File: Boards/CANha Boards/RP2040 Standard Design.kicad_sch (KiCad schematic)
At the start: 37 parts, among them J17 USB_C, J7 BM03B-SRSS-TBLFSN, SW2 SW_Push, SW3 SW_Push, U6 ESD7L5.0DT5G, U7 ST1L05APU33R

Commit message: Algumas correções ERC e ajustes no Design dos DCDC
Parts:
- removed FlashM1: W25Q128JVSIQ_TR, SOIC_208MIL_WIN, symbol W25Q128JVSIQ TR:W25Q128JVSIQ_TR
- removed J17: USB_C, Connector_USB:USB_C_Plug_JAE_DX07P024AJ1, symbol Connector:USB_C_Receptacle_USB2.0
- removed J7: BM03B-SRSS-TBLFSN, CONN_BM03B-SRSS-TBLFSN_JST, symbol SWD Con:BM03B-SRSS-TBLFSN
- removed SW2, SW3: SW_Push, Button_Switch_SMD:SW_Push_1P1T-MP_NO_Horizontal_Alps_SKRTLAE010, symbol Switch:SW_Push
- removed U6: ESD7L5.0DT5G, SOT-723_0P85X1P25_ONS, symbol ESD Protection Diode:ESD7L5.0DT5G
- removed U7: ST1L05APU33R, DFN_5APU33R_STM, symbol LDO 5V.3V3:ST1L05APU33R
- removed XTAL1: ASE-12.000MHZ-LC-T, ASE-3.2X2.5_ABR, symbol AS12MHz:ASE-12.000MHZ-LC-T
- added J17: USB_C_Receptacle_USB2.0_14P, symbol Connector:USB_C_Receptacle_USB2.0_14P
- added J7: BM03B-SRSS-TBLFSN, CONN_BM03B-SRSS-TBLFSN_JST, symbol SWD Connector:BM03B-SRSS-TBLFSN
- added S3, S4: TL3305CF160QG, TL3305CF160QG:SW_TL3305CF160QG, symbol TL3305CF160QG:TL3305CF160QG
- added U18: ST1L05APU33R, DFN_5APU33R_STM, symbol LDO 5V 3V3:ST1L05APU33R
- added U6: W25Q128JVSIQ TR, SOIC_208MIL_WIN, symbol 16MB Flash Memory:W25Q128JVSIQ_TR
- added U7: ESD7L5.0DT5G, SOT-723_0P85X1P25_ONS, symbol ESD Diodes:ESD7L5.0DT5G
- added XTAL1: ASE-12.000MHZ-LC-T, ASE-3.2X2.5_ABR, symbol Powered Crystal:ASE-12.000MHZ-LC-T
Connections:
- net +3.3V: now also U18.2 (V0), U6.8 (VCC), XTAL1.4 (VDD)
- net +5V: now also J17.A4 (VBUS), J17.A9 (VBUS), J17.B4 (VBUS), J17.B9 (VBUS), U18.3 (V1)
- net CRYSTAL: now also XTAL1.3 (OUTPUT)
- net GND: now also J17.A1 (GND), J17.A12 (GND), J17.B1 (GND), J17.B12 (GND), J7.2, S3.2, S4.2, U18.6 (GND), U18.7 (GND), U6.4 (GND), U7.3, XTAL1.2 (GND/CASE)
- net MCU QSPI_SCLK: now also U6.6 (CLK)
- net MCU QSPI_SD0: now also U6.5 (DI(IO0))
- net MCU QSPI_SD1: now also U6.2 (DO(IO1))
- net MCU QSPI_SD2: now also U6.3 (/WP(IO2))
- net MCU QSPI_SD3: now also U6.7 (/HOLD_/RESET)
- net MCU QSPI_SS: now also U6.1 (/CS)
- net USB_DM: now also J17.A7 (D-), J17.B7 (D-), U7.1
- net USB_DP: now also J17.A6 (D+), J17.B6 (D+), U7.2
- net ~{RST}: now also S3.4
- net ~{USB_BOOT}: now also S4.4
- net at R37.1: now also XTAL1.1 (TRI-STATE(STBY))
- net at R25.1: now also J7.3
- net at R35.1: now also J7.1
- net at R39.2: now also J17.A5 (CC1)
- net at RC1.2: now also J17.B5 (CC2)
- no-connect marks 4 -> 6

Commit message: pequenas alterações, implementação do sensor de temperatura na placa de comunicações
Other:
- company: (none) -> Porto Space Team
- title: (none) -> RP2040 Standard
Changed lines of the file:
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@@
 	(generator_version "8.0")
 	(paper "A4")
+	(title_block
+		(title "RP2040 Standard")
+		(company "Porto Space Team")
+		(comment 1 "Miguel Amorim")
+	)
 	(junction
 		(at 45.72 70.485)

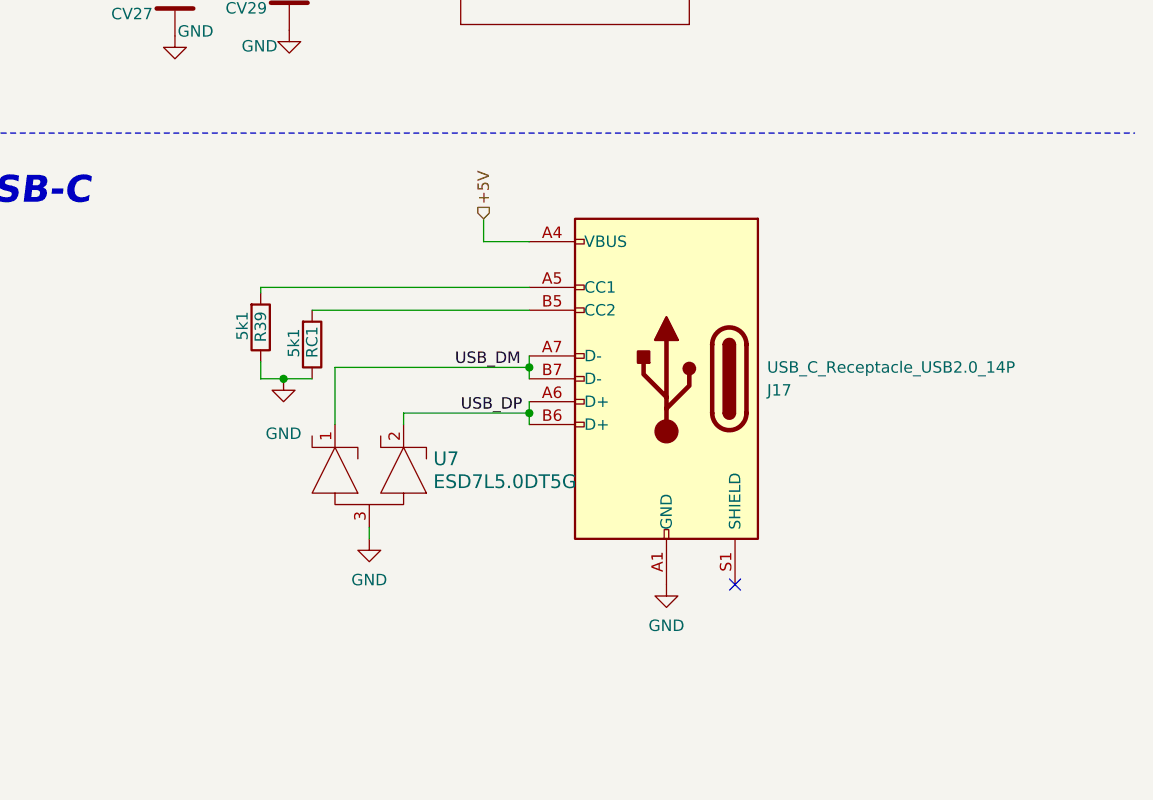
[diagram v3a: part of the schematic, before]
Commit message: USB-C update
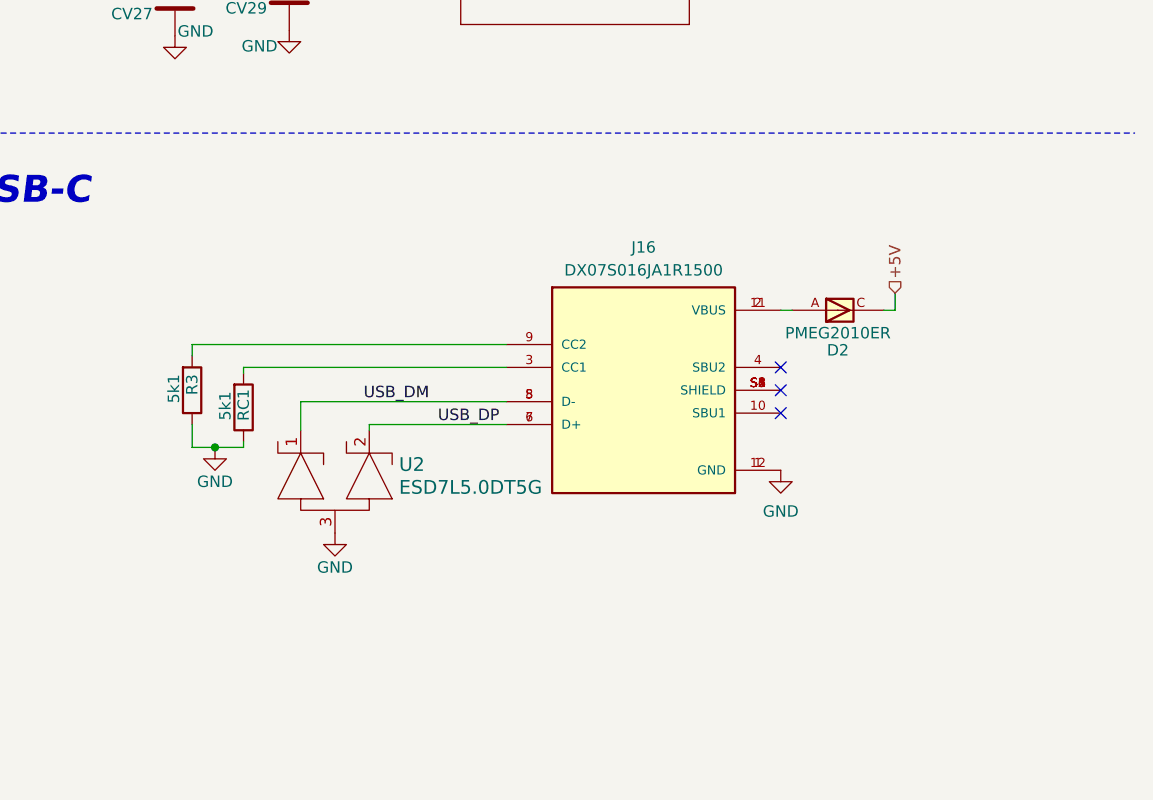
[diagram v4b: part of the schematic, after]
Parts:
- removed J17: USB_C_Receptacle_USB2.0_14P, symbol Connector:USB_C_Receptacle_USB2.0_14P
- removed R39: 5k1, Resistor_SMD:R_0201_0603Metric, symbol Device:R
- removed U7: ESD7L5.0DT5G, SOT-723_0P85X1P25_ONS, symbol ESD Diodes:ESD7L5.0DT5G
- added D2: PMEG2010ER, PMEG2010ER:SODFL3517X110N, symbol Schottky Diode:PMEG2010ER
- added J16: DX07S016JA1R1500, DX07S016JA1R1500:JAE_DX07S016JA1R1500, symbol DX07S016JA1R1500:DX07S016JA1R1500
- added R3: 5k1, Resistor_SMD:R_0201_0603Metric, symbol Device:R
- added U2: ESD7L5.0DT5G, SOT-723_0P85X1P25_ONS, symbol ESD Diodes:ESD7L5.0DT5G
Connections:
- net +5V: now also D2.C
- net GND: now also J16.1 (GND), J16.12 (GND), R3.1, U2.3
- net USB_DM: now also J16.5 (D-), J16.8 (D-), U2.1
- net USB_DP: now also J16.6 (D+), J16.7 (D+), U2.2
- net at RC1.2: now also J16.3 (CC1)
- new net: D2.A, J16.11 (VBUS), J16.2 (VBUS)
- new net: J16.9 (CC2), R3.2
- new net: J16.S1 (SHIELD), J16.S2 (SHIELD), J16.S3 (SHIELD), J16.S4 (SHIELD), J16.S5 (SHIELD), J16.S6 (SHIELD)
- no-connect marks 6 -> 8

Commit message: Atualização CANha
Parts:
- CV13, CV14, CV15, CV16, CV17, CV18, CV19, CV20, CV21, CV22, CV23, CV24, CV25, CV26, CV29, CV30: footprint Capacitor_SMD:C_0201_0603Metric -> CAP_GCM155_MUR:CAP_GCM155_MUR
- CV27, CV28: footprint Capacitor_SMD:C_0201_0603Metric -> GRM15x:GRM15x
- J16: footprint DX07S016JA1R1500:JAE_DX07S016JA1R1500 -> USBC-DX07S016JA1:JAE_DX07S016JA1R1500
- J7: footprint CONN_BM03B-SRSS-TBLFSN_JST -> SWD_Con:CONN_BM03B-SRSS-TBLFSN_JST
- R22, R23, R24, R25, R3, R35, R36, R37, R38: footprint Resistor_SMD:R_0201_0603Metric -> RC0402N_VIS:RC0402N_VIS
- RC1: footprint Resistor_SMD:R_0201_0603Metric -> ERA6AEB101V:ERA6AEB101V
- S3, S4: footprint TL3305CF160QG:SW_TL3305CF160QG -> E-Switch_7mm:SW_TL3305CF160QG
- U18: footprint DFN_5APU33R_STM -> LDO ST1L05A:DFN_5APU33R_STM
- U2: footprint SOT-723_0P85X1P25_ONS -> ESD7L5-Diode:SOT-723_0P85X1P25_ONS
- U6: footprint SOIC_208MIL_WIN -> NOR Flash:SOIC_208MIL_WIN
- XTAL1: footprint ASE-3.2X2.5_ABR -> AS12MHz:ASE-3.2X2.5_ABR
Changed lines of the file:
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@@
 			)
 		)
-		(property "Footprint" "Capacitor_SMD:C_0201_0603Metric"
+		(property "Footprint" "CAP_GCM155_MUR:CAP_GCM155_MUR"
 			(at 129.2352 50.165 0)
 			(effects
@@
 			)
 		)
-		(property "Footprint" "Capacitor_SMD:C_0201_0603Metric"
+		(property "Footprint" "CAP_GCM155_MUR:CAP_GCM155_MUR"
 			(at 87.3252 50.165 0)
 			(effects
@@
 			)
 		)
-		(property "Footprint" "Capacitor_SMD:C_0201_0603Metric"
+		(property "Footprint" "CAP_GCM155_MUR:CAP_GCM155_MUR"
 			(at 56.8198 42.545 0)
 			(effects
@@
 			)
 		)
-		(property "Footprint" "Capacitor_SMD:C_0201_0603Metric"
+		(property "Footprint" "CAP_GCM155_MUR:CAP_GCM155_MUR"
 			(at 94.3102 50.165 0)
 			(effects
@@
 			)
 		)
-		(property "Footprint" "Capacitor_SMD:C_0201_0603Metric"
+		(property "Footprint" "CAP_GCM155_MUR:CAP_GCM155_MUR"
 			(at 132.08 177.4698 0)
 			(effects
@@
 			)
 		)
-		(property "Footprint" "DX07S016JA1R1500:JAE_DX07S016JA1R1500"
+		(property "Footprint" "USBC-DX07S016JA1:JAE_DX07S016JA1R1500"
 			(at 230.505 135.89 0)
 			(effects
@@
 			)
 		)
-		(property "Footprint" "Capacitor_SMD:C_0201_0603Metric"
+		(property "Footprint" "CAP_GCM155_MUR:CAP_GCM155_MUR"
 			(at 115.2652 50.165 0)
 			(effects
@@
 			)
 		)
-		(property "Footprint" "Capacitor_SMD:C_0201_0603Metric"
+		(property "Footprint" "CAP_GCM155_MUR:CAP_GCM155_MUR"
 			(at 101.2952 50.165 0)
 			(effects
@@
 			)
 		)
-		(property "Footprint" "SOIC_208MIL_WIN"
+		(property "Footprint" "NOR Flash:SOIC_208MIL_WIN"
 			(at 180.975 45.72 0)
 			(effects
@@
 			)
 		)
-		(property "Footprint" "CONN_BM03B-SRSS-TBLFSN_JST"
+		(property "Footprint" "SWD_Con:CONN_BM03B-SRSS-TBLFSN_JST"
 			(at 35.56 140.335 0)
 			(effects
@@
 			)
 		)
-		(property "Footprint" "Capacitor_SMD:C_0201_0603Metric"
+		(property "Footprint" "GRM15x:GRM15x"
 			(at 177.4698 90.17 0)
 			(effects
@@
 			)
 		)
-		(property "Footprint" "TL3305CF160QG:SW_TL3305CF160QG"
+		(property "Footprint" "E-Switch_7mm:SW_TL3305CF160QG"
 			(at 33.02 50.8 0)
 			(effects
@@
 			)
 		)
-		(property "Footprint" "Capacitor_SMD:C_0201_0603Metric"
+		(property "Footprint" "CAP_GCM155_MUR:CAP_GCM155_MUR"
 			(at 190.1698 89.535 0)
 			(effects
@@
 			)
 		)
-		(property "Footprint" "TL3305CF160QG:SW_TL3305CF160QG"
+		(property "Footprint" "E-Switch_7mm:SW_TL3305CF160QG"
 			(at 161.925 31.75 0)
 			(effects
@@
 			)
 		)
-		(property "Footprint" "Resistor_SMD:R_0201_0603Metric"
+		(property "Footprint" "ERA6AEB101V:ERA6AEB101V"
 			(at 184.277 139.065 90)
 			(effects
@@
 			)
 		)
-		(property "Footprint" "Resistor_SMD:R_0201_0603Metric"
+		(property "Footprint" "RC0402N_VIS:RC0402N_VIS"
 			(at 41.275 78.867 90)
 			(effects
@@
 			)
 		)
-		(property "Footprint" "Resistor_SMD:R_0201_0603Metric"
+		(property "Footprint" "RC0402N_VIS:RC0402N_VIS"
 			(at 41.275 79.883 90)
 			(effects
@@
 			)
 		)
-		(property "Footprint" "Resistor_SMD:R_0201_0603Metric"
+		(property "Footprint" "RC0402N_VIS:RC0402N_VIS"
 			(at 43.942 64.77 90)
 			(effects
@@
 			)
 		)
-		(property "Footprint" "Capacitor_SMD:C_0201_0603Metric"
+		(property "Footprint" "CAP_GCM155_MUR:CAP_GCM155_MUR"
 			(at 136.2202 50.165 0)
 			(effects
@@
 			)
 		)
-		(property "Footprint" "ASE-3.2X2.5_ABR"
+		(property "Footprint" "AS12MHz:ASE-3.2X2.5_ABR"
 			(at 57.15 182.88 0)
 			(effects
@@
 			)
 		)
-		(property "Footprint" "Resistor_SMD:R_0201_0603Metric"
+		(property "Footprint" "RC0402N_VIS:RC0402N_VIS"
 			(at 55.372 177.8 90)
 			(effects
@@
 			)
 		)
-		(property "Footprint" "Resistor_SMD:R_0201_0603Metric"
+		(property "Footprint" "RC0402N_VIS:RC0402N_VIS"
 			(at 41.91 138.557 90)
 			(effects
@@
 			)
 		)
-		(property "Footprint" "SOT-723_0P85X1P25_ONS"
+		(property "Footprint" "ESD7L5-Diode:SOT-723_0P85X1P25_ONS"
 			(at 197.485 137.795 0)
 			(effects
@@
 			)
 		)
-		(property "Footprint" "Capacitor_SMD:C_0201_0603Metric"
+		(property "Footprint" "CAP_GCM155_MUR:CAP_GCM155_MUR"
 			(at 32.6898 61.595 0)
 			(effects
@@
 			)
 		)
-		(property "Footprint" "Capacitor_SMD:C_0201_0603Metric"
+		(property "Footprint" "CAP_GCM155_MUR:CAP_GCM155_MUR"
 			(at 272.7452 41.91 0)
 			(effects
@@
 			)
 		)
-		(property "Footprint" "Resistor_SMD:R_0201_0603Metric"
+		(property "Footprint" "RC0402N_VIS:RC0402N_VIS"
 			(at 18.542 65.405 90)
 			(effects
@@
 			)
 		)
-		(property "Footprint" "Resistor_SMD:R_0201_0603Metric"
+		(property "Footprint" "RC0402N_VIS:RC0402N_VIS"
 			(at 41.91 133.477 90)
 			(effects
@@
 			)
 		)
-		(property "Footprint" "Capacitor_SMD:C_0201_0603Metric"
+		(property "Footprint" "CAP_GCM155_MUR:CAP_GCM155_MUR"
 			(at 87.3252 59.69 0)
 			(effects
@@
 			)
 		)
-		(property "Footprint" "Capacitor_SMD:C_0201_0603Metric"
+		(property "Footprint" "GRM15x:GRM15x"
 			(at 190.1698 85.725 0)
 			(effects
@@
 			)
 		)
-		(property "Footprint" "Capacitor_SMD:C_0201_0603Metric"
+		(property "Footprint" "CAP_GCM155_MUR:CAP_GCM155_MUR"
 			(at 108.2802 50.165 0)
 			(effects
@@
 			)
 		)
-		(property "Footprint" "Capacitor_SMD:C_0201_0603Metric"
+		(property "Footprint" "CAP_GCM155_MUR:CAP_GCM155_MUR"
 			(at 64.4652 62.23 0)
 			(effects
@@
 			)
 		)
-		(property "Footprint" "Resistor_SMD:R_0201_0603Metric"
+		(property "Footprint" "RC0402N_VIS:RC0402N_VIS"
 			(at 178.562 137.16 90)
 			(effects
@@
 			)
 		)
-		(property "Footprint" "Capacitor_SMD:C_0201_0603Metric"
+		(property "Footprint" "CAP_GCM155_MUR:CAP_GCM155_MUR"
 			(at 64.4398 42.545 0)
 			(effects
@@
 			)
 		)
-		(property "Footprint" "Resistor_SMD:R_0201_0603Metric"
+		(property "Footprint" "RC0402N_VIS:RC0402N_VIS"
 			(at 177.927 40.005 90)
 			(effects
@@
 			)
 		)
-		(property "Footprint" "DFN_5APU33R_STM"
+		(property "Footprint" "LDO ST1L05A:DFN_5APU33R_STM"
 			(at 202.565 83.82 0)
 			(effects
@@
 			)
 		)
-		(property "Footprint" "Capacitor_SMD:C_0201_0603Metric"
+		(property "Footprint" "CAP_GCM155_MUR:CAP_GCM155_MUR"
 			(at 122.2502 50.165 0)
 			(effects

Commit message: Mudança de nome das footprints
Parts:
- CV13, CV14, CV15, CV16, CV17, CV18, CV19, CV20, CV21, CV22, CV23, CV24, CV25, CV26, CV29, CV30: footprint CAP_GCM155_MUR:CAP_GCM155_MUR -> Capacitor_0402:Capacitor_0402
- CV27, CV28: footprint GRM15x:GRM15x -> C_4uF7_0402:C_4uF7_0402
- R22, R25, R35, R36, R37, R38: footprint RC0402N_VIS:RC0402N_VIS -> RES_0402:RES_0402
- R23, R24: footprint RC0402N_VIS:RC0402N_VIS -> RES_R0603_27:RES_R0603_27
- R3: footprint RC0402N_VIS:RC0402N_VIS -> R_0805_5K1:R_0805_5K1
- RC1: footprint ERA6AEB101V:ERA6AEB101V -> R_0805_5K1:R_0805_5K1
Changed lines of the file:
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@@
 			)
 		)
-		(property "Footprint" "CAP_GCM155_MUR:CAP_GCM155_MUR"
+		(property "Footprint" "Capacitor_0402:Capacitor_0402"
 			(at 129.2352 50.165 0)
 			(effects
@@
 			)
 		)
-		(property "Footprint" "CAP_GCM155_MUR:CAP_GCM155_MUR"
+		(property "Footprint" "Capacitor_0402:Capacitor_0402"
 			(at 87.3252 50.165 0)
 			(effects
@@
 			)
 		)
-		(property "Footprint" "CAP_GCM155_MUR:CAP_GCM155_MUR"
+		(property "Footprint" "Capacitor_0402:Capacitor_0402"
 			(at 56.8198 42.545 0)
 			(effects
@@
 			)
 		)
-		(property "Footprint" "CAP_GCM155_MUR:CAP_GCM155_MUR"
+		(property "Footprint" "Capacitor_0402:Capacitor_0402"
 			(at 94.3102 50.165 0)
 			(effects
@@
 			)
 		)
-		(property "Footprint" "CAP_GCM155_MUR:CAP_GCM155_MUR"
+		(property "Footprint" "Capacitor_0402:Capacitor_0402"
 			(at 132.08 177.4698 0)
 			(effects
@@
 			)
 		)
-		(property "Footprint" "CAP_GCM155_MUR:CAP_GCM155_MUR"
+		(property "Footprint" "Capacitor_0402:Capacitor_0402"
 			(at 115.2652 50.165 0)
 			(effects
@@
 			)
 		)
-		(property "Footprint" "CAP_GCM155_MUR:CAP_GCM155_MUR"
+		(property "Footprint" "Capacitor_0402:Capacitor_0402"
 			(at 101.2952 50.165 0)
 			(effects
@@
 			)
 		)
-		(property "Footprint" "GRM15x:GRM15x"
+		(property "Footprint" "C_4uF7_0402:C_4uF7_0402"
 			(at 177.4698 90.17 0)
 			(effects
@@
 			)
 		)
-		(property "Footprint" "CAP_GCM155_MUR:CAP_GCM155_MUR"
+		(property "Footprint" "Capacitor_0402:Capacitor_0402"
 			(at 190.1698 89.535 0)
 			(effects
@@
 			)
 		)
-		(property "Footprint" "ERA6AEB101V:ERA6AEB101V"
+		(property "Footprint" "R_0805_5K1:R_0805_5K1"
 			(at 184.277 139.065 90)
 			(effects
@@
 			)
 		)
-		(property "Footprint" "RC0402N_VIS:RC0402N_VIS"
+		(property "Footprint" "RES_R0603_27:RES_R0603_27"
 			(at 41.275 78.867 90)
 			(effects
@@
 			)
 		)
-		(property "Footprint" "RC0402N_VIS:RC0402N_VIS"
+		(property "Footprint" "RES_R0603_27:RES_R0603_27"
 			(at 41.275 79.883 90)
 			(effects
@@
 			)
 		)
-		(property "Footprint" "RC0402N_VIS:RC0402N_VIS"
+		(property "Footprint" "RES_0402:RES_0402"
 			(at 43.942 64.77 90)
 			(effects
@@
 			)
 		)
-		(property "Footprint" "CAP_GCM155_MUR:CAP_GCM155_MUR"
+		(property "Footprint" "Capacitor_0402:Capacitor_0402"
 			(at 136.2202 50.165 0)
 			(effects
@@
 			)
 		)
-		(property "Footprint" "RC0402N_VIS:RC0402N_VIS"
+		(property "Footprint" "RES_0402:RES_0402"
 			(at 55.372 177.8 90)
 			(effects
@@
 			)
 		)
-		(property "Footprint" "RC0402N_VIS:RC0402N_VIS"
+		(property "Footprint" "RES_0402:RES_0402"
 			(at 41.91 138.557 90)
 			(effects
@@
 			)
 		)
-		(property "Footprint" "CAP_GCM155_MUR:CAP_GCM155_MUR"
+		(property "Footprint" "Capacitor_0402:Capacitor_0402"
 			(at 32.6898 61.595 0)
 			(effects
@@
 			)
 		)
-		(property "Footprint" "CAP_GCM155_MUR:CAP_GCM155_MUR"
+		(property "Footprint" "Capacitor_0402:Capacitor_0402"
 			(at 272.7452 41.91 0)
 			(effects
@@
 			)
 		)
-		(property "Footprint" "RC0402N_VIS:RC0402N_VIS"
+		(property "Footprint" "RES_0402:RES_0402"
 			(at 18.542 65.405 90)
 			(effects
@@
 			)
 		)
-		(property "Footprint" "RC0402N_VIS:RC0402N_VIS"
+		(property "Footprint" "RES_0402:RES_0402"
 			(at 41.91 133.477 90)
 			(effects
@@
 			)
 		)
-		(property "Footprint" "CAP_GCM155_MUR:CAP_GCM155_MUR"
+		(property "Footprint" "Capacitor_0402:Capacitor_0402"
 			(at 87.3252 59.69 0)
 			(effects
@@
 			)
 		)
-		(property "Footprint" "GRM15x:GRM15x"
+		(property "Footprint" "C_4uF7_0402:C_4uF7_0402"
 			(at 190.1698 85.725 0)
 			(effects
@@
 			)
 		)
-		(property "Footprint" "CAP_GCM155_MUR:CAP_GCM155_MUR"
+		(property "Footprint" "Capacitor_0402:Capacitor_0402"
 			(at 108.2802 50.165 0)
 			(effects
@@
 			)
 		)
-		(property "Footprint" "CAP_GCM155_MUR:CAP_GCM155_MUR"
+		(property "Footprint" "Capacitor_0402:Capacitor_0402"
 			(at 64.4652 62.23 0)
 			(effects
@@
 			)
 		)
-		(property "Footprint" "RC0402N_VIS:RC0402N_VIS"
+		(property "Footprint" "R_0805_5K1:R_0805_5K1"
 			(at 178.562 137.16 90)
 			(effects
@@
 			)
 		)
-		(property "Footprint" "CAP_GCM155_MUR:CAP_GCM155_MUR"
+		(property "Footprint" "Capacitor_0402:Capacitor_0402"
 			(at 64.4398 42.545 0)
 			(effects
@@
 			)
 		)
-		(property "Footprint" "RC0402N_VIS:RC0402N_VIS"
+		(property "Footprint" "RES_0402:RES_0402"
 			(at 177.927 40.005 90)
 			(effects
@@
 			)
 		)
-		(property "Footprint" "CAP_GCM155_MUR:CAP_GCM155_MUR"
+		(property "Footprint" "Capacitor_0402:Capacitor_0402"
 			(at 122.2502 50.165 0)
 			(effects
